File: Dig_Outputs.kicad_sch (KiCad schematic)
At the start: 25 parts, among them Q1 MMBT3904, Q2 MMBT3904, Q3 MMBT3904, Q4 MMBT3904

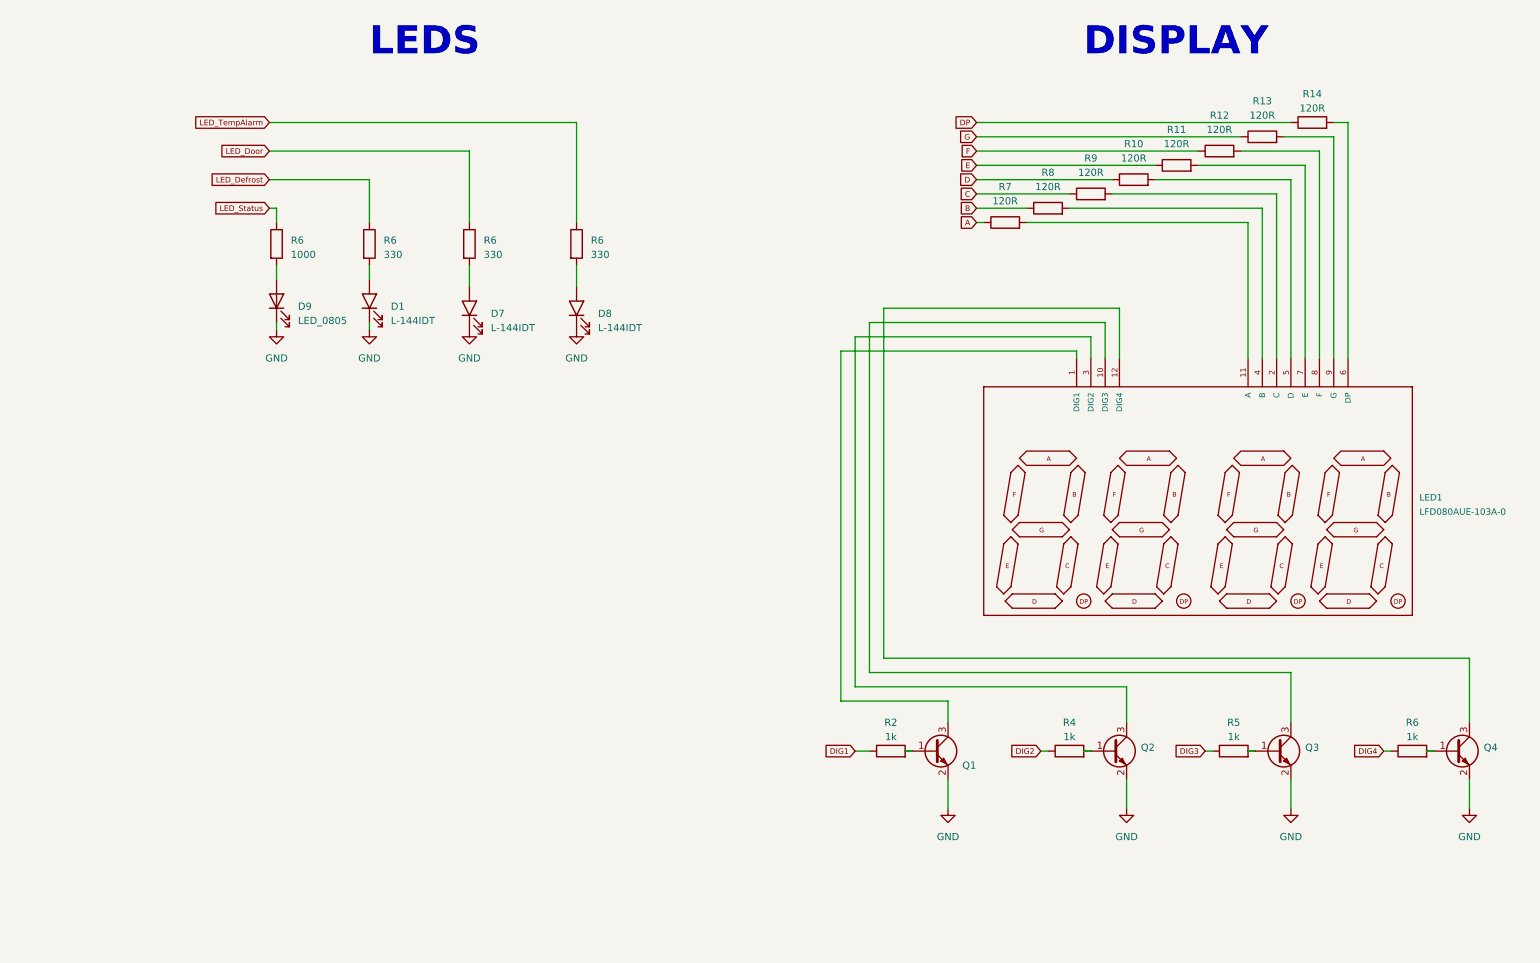
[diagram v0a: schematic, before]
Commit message: SCH: Se cambió el IRM, se colocó filtro en la entrada AC, se modificó la fuente switching LM, se corrigieron algunos errores de diseño. PCB: Se terminó el placement de los componentes
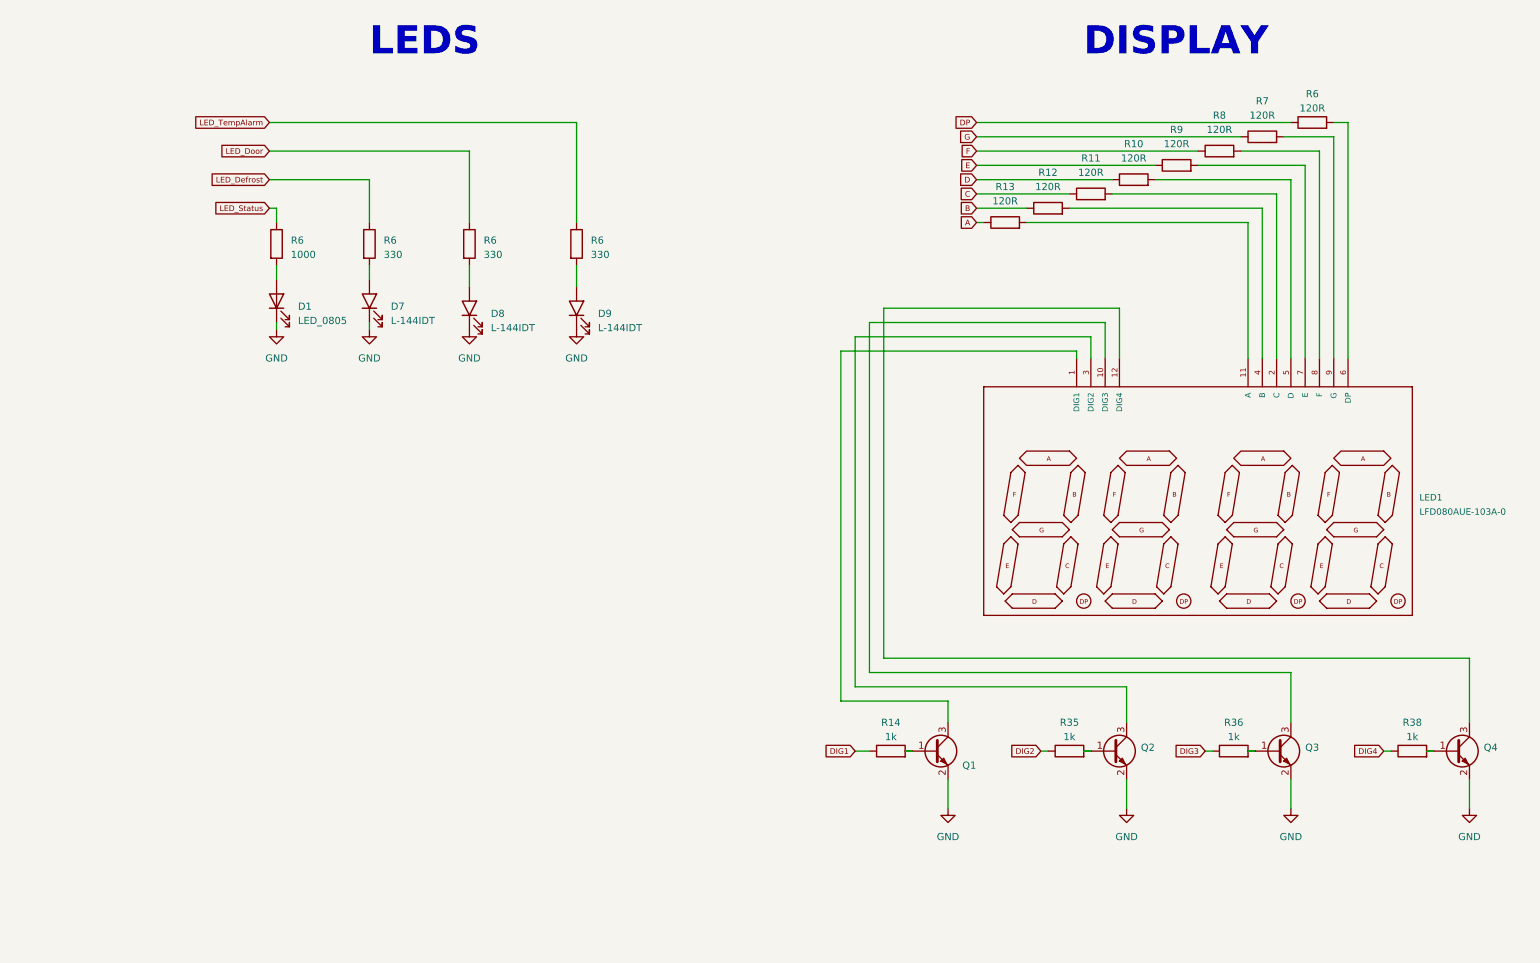
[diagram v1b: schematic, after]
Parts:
- renumbered D9 to D1, D1 to D7, D7 to D8, D8 to D9, R9 to R11, R8 to R12, R7 to R13, R2 to R14, R4 to R35, R5 to R36, R6 to R38, R14 to R6, R13 to R7, R12 to R8, R11 to R9

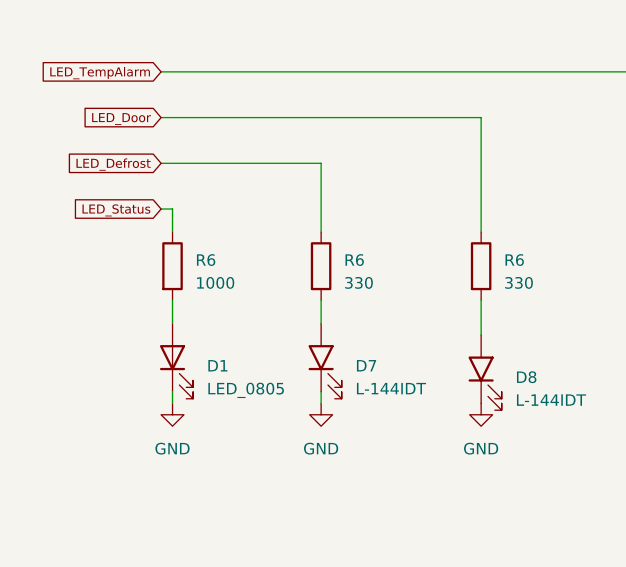
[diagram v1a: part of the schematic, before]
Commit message: SCH: Se modicaron algunos valores y comentarios del sch. PCB: Posiblemente debido a jlcpcb. JLCPCB: Se asigna el código para la soldura
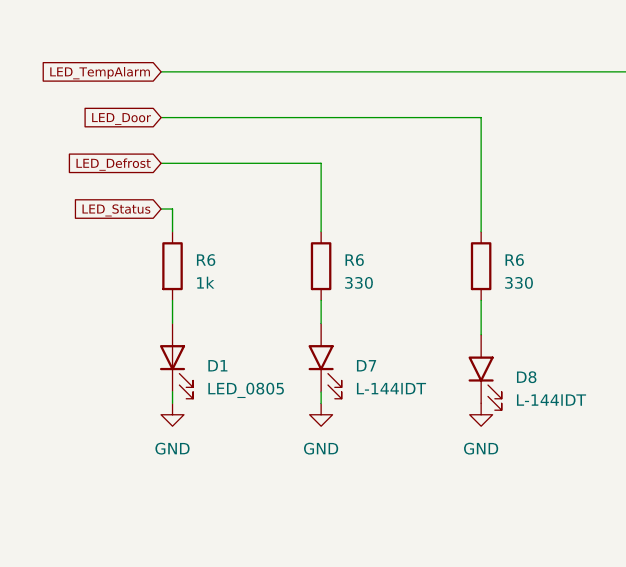
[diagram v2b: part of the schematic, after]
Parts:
- R6: value 1000 -> 1k
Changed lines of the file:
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@@
       (effects (font (size 1.27 1.27)) (justify left))
     )
-    (property "Value" "1000" (at 60.96 59.055 0)
+    (property "Value" "1k" (at 60.96 59.055 0)
       (effects (font (size 1.27 1.27)) (justify left))
     )

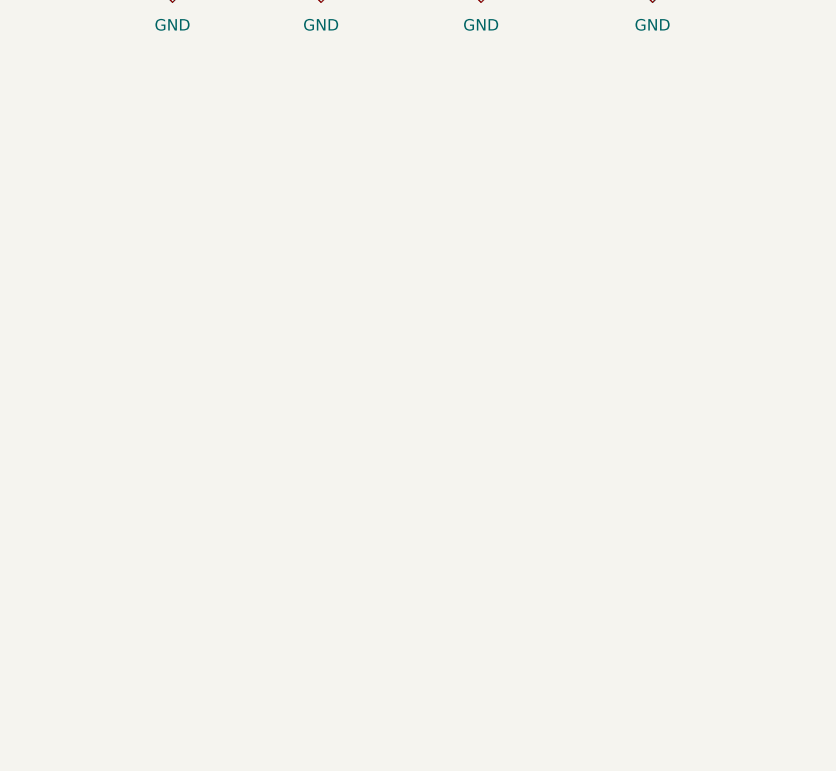
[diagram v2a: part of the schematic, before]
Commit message: SCH: Se arregló la posición de los pulsadores, se agrega buzzer, PCB: Se revisan los componentes y se agrega serigrafía. JLCPCB: Actualizado
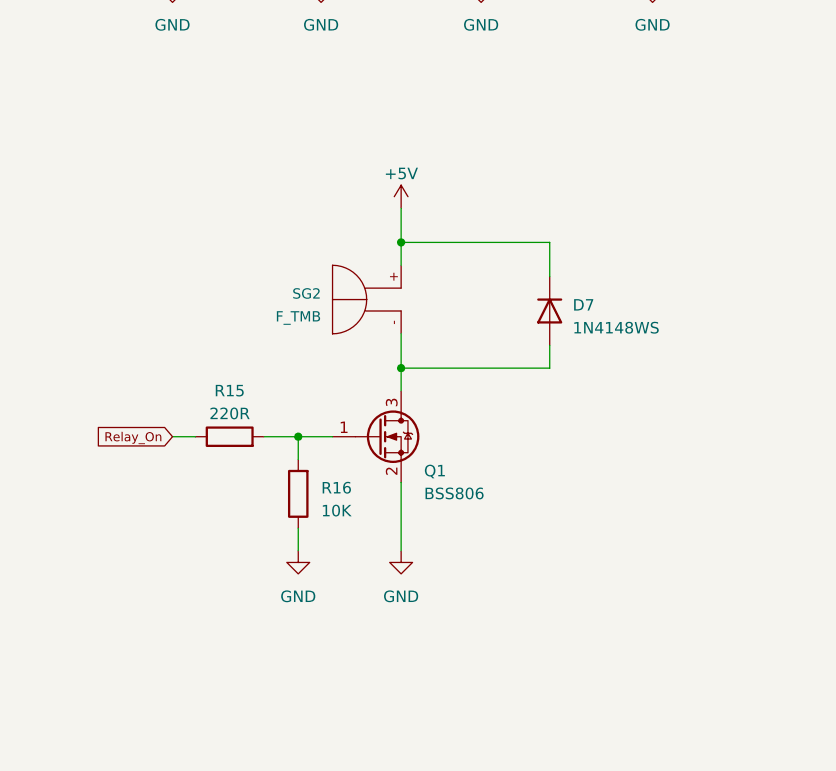
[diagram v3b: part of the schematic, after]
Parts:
- added D7: 1N4148WS, Diode_SMD:D_SOD-323, symbol Diode:1N4148WS
- added Q1: BSS806, Package_TO_SOT_SMD:SOT-23, symbol Transistor_FET:BSS123
- added R15: 220R, 1-Resistor:R_0805_2012Metric, symbol 1-Resistor:R_0805
- added R16: 10K, 1-Resistor:R_0805_2012Metric, symbol 1-Resistor:R_0805
- added SG2: F_TMB, 1-Buzzer-and-Speaker-Eagle:F_TMB, symbol 1-Buzzer-and-Speaker-Eagle:F_TMB
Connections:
- net GND: now also Q1.2 (S), R16.1
- new net: Q1.1 (G), R15.2, R16.2
- new net: D7.2 (A), Q1.3 (D), SG2.-
- new net +5V: D7.1 (K), SG2.+
- new net Relay_On: R15.1

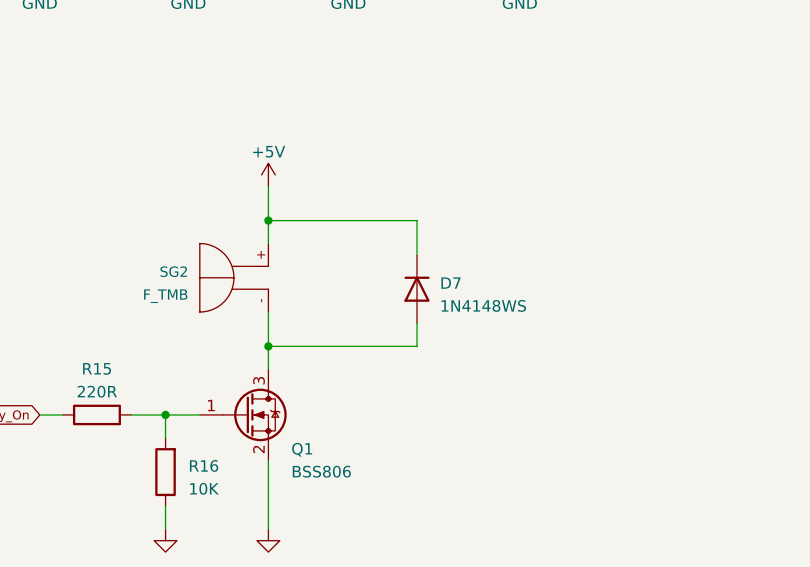
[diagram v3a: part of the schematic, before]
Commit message: SCH: pin EN se corrige para activar la alimentación de 5V, se cambia el empaquetado de varias resistencias 0603 a 0805. PCB: Se alarga el plano de GND, se acomodan los componentes 0805, se completa de colocar la serigrafía, se ensancha la pista de AC. JLCPCB: Se actualiza
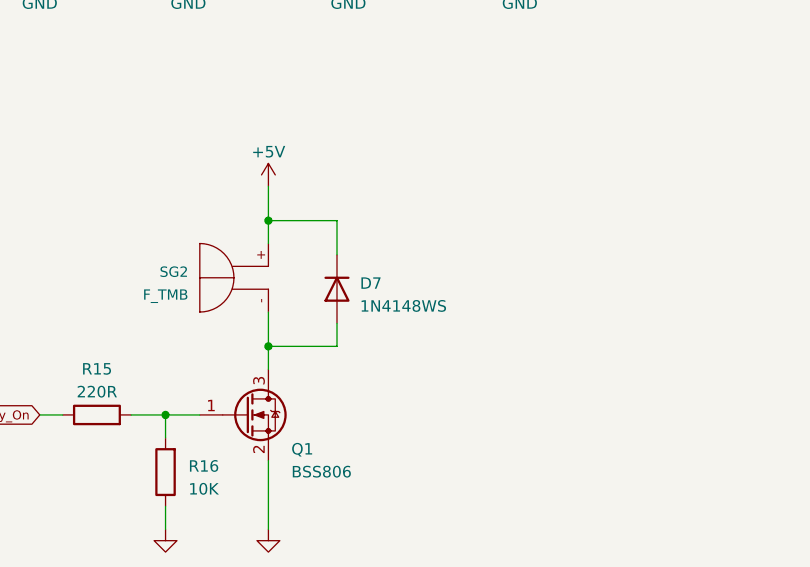
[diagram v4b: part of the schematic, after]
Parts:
- R10, R11, R12, R13, R14, R35, R36, R38, R6, R7, R8, R9: footprint 1-Resistor:R_0603_1608Metric -> 1-Resistor:R_0805_2012Metric
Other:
- moved on the sheet: D7
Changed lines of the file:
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@@
     (stroke (width 0) (type default))
   )
-  (wire (pts (xy 100.33 105.41) (xy 100.33 101.6))
+  (wire (pts (xy 91.44 105.41) (xy 91.44 101.6))
     (stroke (width 0) (type default))
   )
@@
     (stroke (width 0) (type default))
   )
-  (wire (pts (xy 100.33 113.03) (xy 100.33 115.57))
+  (wire (pts (xy 91.44 113.03) (xy 91.44 115.57))
     (stroke (width 0) (type default))
   )
@@
     (stroke (width 0) (type default))
   )
-  (wire (pts (xy 100.33 101.6) (xy 83.82 101.6))
+  (wire (pts (xy 91.44 101.6) (xy 83.82 101.6))
     (stroke (width 0) (type default))
   )
@@
     (stroke (width 0) (type default))
   )
-  (wire (pts (xy 100.33 115.57) (xy 83.82 115.57))
+  (wire (pts (xy 91.44 115.57) (xy 83.82 115.57))
     (stroke (width 0) (type default))
   )
@@
       (effects (font (size 1.27 1.27)))
     )
-    (property "Footprint" "1-Resistor:R_0603_1608Metric" (at 226.06 42.418 90)
+    (property "Footprint" "1-Resistor:R_0805_2012Metric" (at 226.06 42.418 90)
       (effects (font (size 1.27 1.27)) hide)
     )
@@
       (effects (font (size 1.27 1.27)))
     )
-    (property "Footprint" "1-Resistor:R_0603_1608Metric" (at 203.2 50.038 90)
+    (property "Footprint" "1-Resistor:R_0805_2012Metric" (at 203.2 50.038 90)
       (effects (font (size 1.27 1.27)) hide)
     )
@@
       (effects (font (size 1.27 1.27)))
     )
-    (property "Footprint" "1-Resistor:R_0603_1608Metric" (at 242.57 37.338 90)
+    (property "Footprint" "1-Resistor:R_0805_2012Metric" (at 242.57 37.338 90)
       (effects (font (size 1.27 1.27)) hide)
     )
@@
       (effects (font (size 1.27 1.27)) (justify left))
     )
-    (property "Footprint" "1-Resistor:R_0603_1608Metric" (at 56.642 57.15 90)
+    (property "Footprint" "1-Resistor:R_0805_2012Metric" (at 56.642 57.15 90)
       (effects (font (size 1.27 1.27)) hide)
     )
@@
       (effects (font (size 1.27 1.27)) (justify left))
     )
-    (property "Footprint" "1-Resistor:R_0603_1608Metric" (at 90.932 57.15 90)
+    (property "Footprint" "1-Resistor:R_0805_2012Metric" (at 90.932 57.15 90)
       (effects (font (size 1.27 1.27)) hide)
     )
@@
       (effects (font (size 1.27 1.27)) (justify left))
     )
-    (property "Footprint" "1-Resistor:R_0603_1608Metric" (at 109.982 57.15 90)
+    (property "Footprint" "1-Resistor:R_0805_2012Metric" (at 109.982 57.15 90)
       (effects (font (size 1.27 1.27)) hide)
     )
@@
       (effects (font (size 1.27 1.27)))
     )
-    (property "Footprint" "1-Resistor:R_0603_1608Metric" (at 228.6 149.098 90)
+    (property "Footprint" "1-Resistor:R_0805_2012Metric" (at 228.6 149.098 90)
       (effects (font (size 1.27 1.27)) hide)
     )
@@
     )
   )
-  (symbol (lib_id "Diode:1N4148WS") (at 100.33 109.22 90) (mirror x) (unit 1)
+  (symbol (lib_id "Diode:1N4148WS") (at 91.44 109.22 90) (mirror x) (unit 1)
     (in_bom yes) (on_board yes) (dnp no)
-    (property "Reference" "D7" (at 102.87 108.585 90)
+    (property "Reference" "D7" (at 93.98 108.585 90)
       (effects (font (size 1.27 1.27)) (justify right))
     )
-    (property "Value" "1N4148WS" (at 102.87 111.125 90)
+    (property "Value" "1N4148WS" (at 93.98 111.125 90)
       (effects (font (size 1.27 1.27)) (justify right))
     )
-    (property "Footprint" "Diode_SMD:D_SOD-323" (at 104.775 109.22 0)
-      (effects (font (size 1.27 1.27)) hide)
-    )
-    (property "Datasheet" "https://www.vishay.com/docs/85751/1n4148ws.pdf" (at 100.33 109.22 0)
-      (effects (font (size 1.27 1.27)) hide)
-    )
-    (property "Sim.Device" "D" (at 100.33 109.22 0)
-      (effects (font (size 1.27 1.27)) hide)
-    )
-    (property "Sim.Pins" "1=K 2=A" (at 100.33 109.22 0)
+    (property "Footprint" "Diode_SMD:D_SOD-323" (at 95.885 109.22 0)
+      (effects (font (size 1.27 1.27)) hide)
+    )
+    (property "Datasheet" "https://www.vishay.com/docs/85751/1n4148ws.pdf" (at 91.44 109.22 0)
+      (effects (font (size 1.27 1.27)) hide)
+    )
+    (property "Sim.Device" "D" (at 91.44 109.22 0)
+      (effects (font (size 1.27 1.27)) hide)
+    )
+    (property "Sim.Pins" "1=K 2=A" (at 91.44 109.22 0)
       (effects (font (size 1.27 1.27)) hide)
     )
@@
       (effects (font (size 1.27 1.27)))
     )
-    (property "Footprint" "1-Resistor:R_0603_1608Metric" (at 210.82 47.498 90)
+    (property "Footprint" "1-Resistor:R_0805_2012Metric" (at 210.82 47.498 90)
       (effects (font (size 1.27 1.27)) hide)
     )
@@
       (effects (font (size 1.27 1.27)))
     )
-    (property "Footprint" "1-Resistor:R_0603_1608Metric" (at 195.58 52.578 90)
+    (property "Footprint" "1-Resistor:R_0805_2012Metric" (at 195.58 52.578 90)
       (effects (font (size 1.27 1.27)) hide)
     )
@@
       (effects (font (size 1.27 1.27)))
     )
-    (property "Footprint" "1-Resistor:R_0603_1608Metric" (at 233.68 39.878 90)
+    (property "Footprint" "1-Resistor:R_0805_2012Metric" (at 233.68 39.878 90)
       (effects (font (size 1.27 1.27)) hide)
     )
@@
       (effects (font (size 1.27 1.27)))
     )
-    (property "Footprint" "1-Resistor:R_0603_1608Metric" (at 260.35 149.098 90)
+    (property "Footprint" "1-Resistor:R_0805_2012Metric" (at 260.35 149.098 90)
       (effects (font (size 1.27 1.27)) hide)
     )
@@
       (effects (font (size 1.27 1.27)))
     )
-    (property "Footprint" "1-Resistor:R_0603_1608Metric" (at 218.44 44.958 90)
+    (property "Footprint" "1-Resistor:R_0805_2012Metric" (at 218.44 44.958 90)
       (effects (font (size 1.27 1.27)) hide)
     )
@@
       (effects (font (size 1.27 1.27)))
     )
-    (property "Footprint" "1-Resistor:R_0603_1608Metric" (at 187.96 55.118 90)
+    (property "Footprint" "1-Resistor:R_0805_2012Metric" (at 187.96 55.118 90)
       (effects (font (size 1.27 1.27)) hide)
     )
@@
       (effects (font (size 1.27 1.27)))
     )
-    (property "Footprint" "1-Resistor:R_0603_1608Metric" (at 199.39 149.098 90)
+    (property "Footprint" "1-Resistor:R_0805_2012Metric" (at 199.39 149.098 90)
       (effects (font (size 1.27 1.27)) hide)
     )
@@
       (effects (font (size 1.27 1.27)))
     )
-    (property "Footprint" "1-Resistor:R_0603_1608Metric" (at 167.64 149.098 90)
+    (property "Footprint" "1-Resistor:R_0805_2012Metric" (at 167.64 149.098 90)
       (effects (font (size 1.27 1.27)) hide)
     )
@@
       (effects (font (size 1.27 1.27)) (justify left))
     )
-    (property "Footprint" "1-Resistor:R_0603_1608Metric" (at 73.152 57.15 90)
-      (effects (font (size 1.27 1.27)) hide)
-    )
+    (property "Footprint" "1-Resistor:R_0805_2012Metric" (at 73.152 57.15 90)
+      (effects (font (size 1.27 1.27)) hide)
+    )
